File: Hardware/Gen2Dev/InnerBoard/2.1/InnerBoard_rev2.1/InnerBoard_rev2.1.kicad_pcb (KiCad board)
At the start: 2 copper layers, 18 parts, among them J1 SI-46020-F, J2 HMTSW-102-X-X-S-X, J7 USB_C_Receptacle, J8 1051620001, SW1 PTS815 SJM 250 SMTR LFS, SW2 PTS815 SJM 250 SMTR LFS

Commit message: stuff
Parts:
- added C31: 10uF, Capacitor_SMD:C_0805_2012Metric, F.Cu at (188.5, -25.2)
- added D11: LED, LED_SMD:LED_0603_1608Metric, F.Cu at (192.7, -22.6)
- added D12: PMEG6010CEJ, Diode_SMD:D_SOD-323F, F.Cu at (207.1, -45.3)
- added D13: 1N5819WS, Diode_SMD:D_SOD-323, F.Cu at (207.1, -42.3)
- added D14: 1N5819WS, Diode_SMD:D_SOD-323, F.Cu at (207.1, -39.4)
- added J3: UJ31-CH-G2-SMT-TR, UJ31-CH-G2-SMT-TR:CUI_UJ31-CH-G2-SMT-TR, F.Cu at (184.9, -45.1)
- added J4: HMTSW-102-X-X-S-X, HMTSW-102-X-X-S-X:SAMTEC_HMTSW-102-X-X-S-X, F.Cu at (201.7, -32.8)
- added J5: UJ31-CH-G2-SMT-TR, UJ31-CH-G2-SMT-TR:CUI_UJ31-CH-G2-SMT-TR, F.Cu at (196.4, -45.1)
- added J6: HMTSW-102-X-X-S-X, HMTSW-102-X-X-S-X:SAMTEC_HMTSW-102-X-X-S-X, F.Cu at (201.7, -28.7)
- added L6: FB0805/600R/2A, Inductor_SMD:L_0805_2012Metric, F.Cu at (193.0, -25.3)
- added R49: 220, Resistor_SMD:R_0805_2012Metric, F.Cu at (184.0, -33.3)
- added R50: 6.1K, Resistor_SMD:R_0805_2012Metric, F.Cu at (184.0, -30.4)
- added R51: 100, Resistor_SMD:R_0805_2012Metric, F.Cu at (184.0, -27.4)
- added TP1: TestPoint, TestPoint:TestPoint_Pad_D2.0mm, F.Cu at (188.3, -32.8)
- added TP2: TestPoint, TestPoint:TestPoint_Pad_D2.0mm, F.Cu at (188.3, -28.7)
- added TP3: TestPoint, TestPoint:TestPoint_Pad_D2.0mm, F.Cu at (192.3, -32.8)
- added TP4: TestPoint, TestPoint:TestPoint_Pad_D2.0mm, F.Cu at (192.3, -28.7)
- added TP5: TestPoint, TestPoint:TestPoint_Pad_D2.0mm, F.Cu at (196.4, -32.8)
- added TP6: TestPoint, TestPoint:TestPoint_Pad_D2.0mm, F.Cu at (196.4, -28.7)
- added U9: FT232RQ, FT232RQ:QFN50P500X500X90-33N, F.Cu at (202.6, -23.1)
- J7: value USB_C_Receptacle -> HMTSW-102-X-X-S-X; footprint Connector_USB:USB_C_Receptacle_Molex_105450-0101-L -> HMTSW-102-X-X-S-X:SAMTEC_HMTSW-102-X-X-S-X
- R24: value 220R/R0402 -> 0; footprint Resistor_SMD:R_0402_1005Metric -> Resistor_SMD:R_0805_2012Metric
- R26: value 10k/R0402 -> 10k; footprint Resistor_SMD:R_0402_1005Metric -> Resistor_SMD:R_0805_2012Metric
- R27: value NA/R0402 -> 5.1K; footprint Resistor_SMD:R_0402_1005Metric -> Resistor_SMD:R_0805_2012Metric
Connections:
- R24 pad 1: Net-(R24-Pad1) -> /D_Com
- R24 pad 2: GND -> Net-(R24-Pad2)
- R26 pad 2: Net-(R26-Pad2) -> Net-(R24-Pad2)
- R27 pad 1: Net-(R26-Pad2) -> Net-(J5-CC1)
- R27 pad 2: /D_Com -> GND
- SW1 pad 2: Net-(R26-Pad2) -> Net-(R24-Pad2)
- SW1 pad 4: Net-(R24-Pad1) -> Net-(R49-Pad1)
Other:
- board outline added: 101.6 x 76.2 mm

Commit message: stuff
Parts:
- added U11: LAN8710A-EZC, LAN8710A_EZC:QFN32_5X5MC_MCH, F.Cu at (192.3, -53.1)
- added U12: TPS2376PW, TPS2376PW:PW8, F.Cu at (179.4, -52.7)
- added U13: RFM-0505S, RFM_0505S:SIP4_RFM_RCP, F.Cu at (177.7, -64.8)
- added U14: TPS54561DPRR, TPS54561DPRR:WSON10_DPR_TEX, F.Cu at (191.6, -67.5)
- added U15: TPS54561DPRR, TPS54561DPRR:WSON10_DPR_TEX, F.Cu at (191.6, -61.7)
- added U16: ROE-0512S, ROE-0512S:ROE_RCP, F.Cu at (177.7, -60.6)

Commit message: stuff
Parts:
- removed J3: UJ31-CH-G2-SMT-TR, UJ31-CH-G2-SMT-TR:CUI_UJ31-CH-G2-SMT-TR
- removed UEXT1: P-B-V-10-LF, 3221-10-0300-00:CONN10_3221-10-0300-00_CNC
- added C24: 18pF, Capacitor_SMD:C_0402_1005Metric, F.Cu at (136.7, -56.1)
- added C25: 100nF, Capacitor_SMD:C_0805_2012Metric, F.Cu at (133.2, -58.6)
- added C29: 18pF, Capacitor_SMD:C_0402_1005Metric, F.Cu at (136.7, -54.1)
- added C32: 1uF, Capacitor_SMD:C_0805_2012Metric, F.Cu at (186.0, -15.7)
- added D10: 1N5819WS, Diode_SMD:D_SOD-323, F.Cu at (133.2, -55.6)
- added D15: BAT54C, Package_TO_SOT_SMD:SOT-23, F.Cu at (124.2, -62.3)
- added Q4: BC817, Package_TO_SOT_SMD:SOT-23, F.Cu at (124.2, -57.9)
- added Q5: BC817, Package_TO_SOT_SMD:SOT-23, F.Cu at (124.2, -53.4)
- added R34: 2.2k, Resistor_SMD:R_0805_2012Metric, F.Cu at (164.8, -20.1)
- added R35: 10, Resistor_SMD:R_0805_2012Metric, F.Cu at (128.8, -63.1)
- added R41: 1k, Resistor_SMD:R_0805_2012Metric, F.Cu at (128.8, -60.1)
- added R42: 10k, Resistor_SMD:R_0805_2012Metric, F.Cu at (164.8, -17.1)
- added R43: 2.2k, Resistor_SMD:R_0805_2012Metric, F.Cu at (164.8, -14.2)
- added R45: 1k, Resistor_SMD:R_0805_2012Metric, F.Cu at (128.8, -57.2)
- added R46: 220, Resistor_SMD:R_0805_2012Metric, F.Cu at (128.8, -54.2)
- added R47: 10k, Resistor_SMD:R_0805_2012Metric, F.Cu at (164.8, -11.2)
- added R52: 10k, Resistor_SMD:R_0805_2012Metric, F.Cu at (186.0, -12.7)
- added TP7: TestPoint, TestPoint:TestPoint_Pad_D2.0mm, F.Cu at (169.0, -19.5)
- added U10: ESP32-WROOM-32E-N8, ESP32_WROOM_32E_N8:ESP32­WROOM­32E_EXP, F.Cu at (176.3, 124.0)
- added U6: 74LVC1G04, Package_TO_SOT_SMD:SOT-23-5, F.Cu at (133.6, -62.3)
- added Y1: ABLS2-12.000MHZ-D4Y-T, ABLS2-12.000MHZ-D4Y-T:XTAL_ABLS2-12.000MHZ-D4Y-T, F.Cu at (130.0, -67.7)
- J8: value 1051620001 -> 3221-10-0300-00; footprint 1051620001:105162-0001_MOL -> 3221-10-0300-00:CONN10_3221-10-0300-00_CNC
- moved J5 194.4 mm to (97.2, 122.0), turned to -90 degrees
- moved U9 175.4 mm to (108.6, 125.0), turned to -90 degrees
- moved J1 123.9 mm to (102.5, 73.3)
- moved U14 5.12 mm to (195.9, -70.3)
- moved U15 3.66 mm to (195.3, -61.4)
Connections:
- R24 pad 1: /D_Com -> D_Com
- SW1 pad 1: /GPI34/BUT1 -> GPI34/BUT1
- SW2 pad 1: /ESP_EN -> ESP_EN
- U9 pad 27: unconnected-(U9-OSCI-Pad27) -> Net-(U9-OSCI)
- U9 pad 28: unconnected-(U9-OSCO-Pad28) -> Net-(U9-OSCO)
- U9 pad 31: unconnected-(U9-~{DTR}-Pad31) -> Net-(Q5-C)
- U9 pad 32: unconnected-(U9-~{RTS}-Pad32) -> Net-(Q4-E)

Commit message: poe
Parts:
- removed J1: SI-46020-F, SI-46020-F:BEL_SI-46020-F
- removed J7: HMTSW-102-X-X-S-X, HMTSW-102-X-X-S-X:SAMTEC_HMTSW-102-X-X-S-X
- added C20: 10uF, Capacitor_SMD:C_0805_2012Metric, F.Cu at (242.4, -57.8)
- added C21: 1uF, Capacitor_SMD:C_0805_2012Metric, F.Cu at (242.4, -54.8)
- added C22: 10uF, Capacitor_SMD:C_0805_2012Metric, F.Cu at (242.4, -51.8)
- added C23: 1uF, Capacitor_SMD:C_0805_2012Metric, F.Cu at (242.4, -48.8)
- added C59: 1nF, Capacitor_SMD:C_0805_2012Metric, F.Cu at (242.4, -45.8)
- added C60: 22uF, Capacitor_SMD:C_0805_2012Metric, F.Cu at (242.4, -42.8)
- added C61: 100nF, Capacitor_SMD:C_0805_2012Metric, F.Cu at (246.9, -57.8)
- added C62: 100nF, Capacitor_SMD:C_0805_2012Metric, F.Cu at (246.9, -54.8)
- added C63: 2.2uF, Capacitor_SMD:C_0805_2012Metric, F.Cu at (246.9, -51.8)
- added C64: 100nF, Capacitor_SMD:C_0805_2012Metric, F.Cu at (246.9, -48.8)
- added C65: 100nF, Capacitor_SMD:C_0805_2012Metric, F.Cu at (246.9, -45.8)
- added C66: 22uF, Capacitor_SMD:C_0805_2012Metric, F.Cu at (246.9, -42.8)
- added C67: 22uF, Capacitor_SMD:C_0805_2012Metric, F.Cu at (251.3, -57.8)
- added C68: 100nF, Capacitor_SMD:C_0805_2012Metric, F.Cu at (251.3, -54.8)
- added C69: 1nF, Capacitor_SMD:C_0805_2012Metric, F.Cu at (251.3, -51.8)
- added C70: 100nF, Capacitor_SMD:C_0805_2012Metric, F.Cu at (251.3, -48.8)
- added C71: 22uF, Capacitor_SMD:C_0805_2012Metric, F.Cu at (251.3, -45.8)
- added C72: 1uF, Capacitor_SMD:C_0805_2012Metric, F.Cu at (270.0, -54.0)
- added D23: SMAJ58A, Diode_SMD:D_SMA, F.Cu at (233.7, -31.8)
- added D24: BAT54A, Package_TO_SOT_SMD:SOT-23, F.Cu at (270.2, -57.7)
- added D4: LED, LED_SMD:LED_0603_1608Metric, F.Cu at (255.6, -58.1)
- added D5: LED, LED_SMD:LED_0603_1608Metric, F.Cu at (255.6, -55.5)
- added D6: 1N5819, Diode_THT:D_DO-41_SOD81_P10.16mm_Horizontal, F.Cu at (242.1, -39.2)
- added D7: LED, LED_SMD:LED_0603_1608Metric, F.Cu at (255.6, -52.9)
- added J3: HMTSW-102-X-X-S-X, HMTSW-102-X-X-S-X:SAMTEC_HMTSW-102-X-X-S-X, F.Cu at (225.9, -36.7)
- added J9: HMTSW-102-X-X-S-X, HMTSW-102-X-X-S-X:SAMTEC_HMTSW-102-X-X-S-X, F.Cu at (225.9, -32.7)
- added L8: 600R/2A, Inductor_SMD:L_0805_2012Metric, F.Cu at (255.8, -50.2)
- added L9: 600R/2A, Inductor_SMD:L_0805_2012Metric, F.Cu at (255.8, -47.5)
- added Q1: SI2323DS-T1-GE3, SI2323DS-T1-GE3:SOT23, F.Cu at (231.7, -36.4)
- added Q10: BSS138, Package_TO_SOT_SMD:SOT-23, F.Cu at (237.3, -27.3)
- added Q9: SI2323DS-T1-GE3, SI2323DS-T1-GE3:SOT23, F.Cu at (235.7, -36.4)
- added R100: 10k, Resistor_SMD:R_0805_2012Metric, F.Cu at (233.6, -40.2)
- added R101: 10k, Resistor_SMD:R_0805_2012Metric, F.Cu at (238.0, -57.9)
- added R104: 2.2k, Resistor_SMD:R_0805_2012Metric, F.Cu at (238.0, -54.9)
- added R105: 2.2k, Resistor_SMD:R_0805_2012Metric, F.Cu at (238.0, -52.0)
- added R106: 2.2k, Resistor_SMD:R_0805_2012Metric, F.Cu at (238.0, -49.0)
- added R107: 2.2k, Resistor_SMD:R_0805_2012Metric, F.Cu at (238.0, -46.1)
- added R108: 49.9k, Resistor_SMD:R_0805_2012Metric, F.Cu at (265.5, -58.5)
- added R109: 100k, Resistor_SMD:R_0805_2012Metric, F.Cu at (265.5, -55.5)
- added R21: 10k, Resistor_SMD:R_0805_2012Metric, F.Cu at (224.8, -57.9)
- added R22: 2.2k, Resistor_SMD:R_0805_2012Metric, F.Cu at (224.8, -54.9)
- added R23: 100, Resistor_SMD:R_0805_2012Metric, F.Cu at (224.8, -52.0)
- added R25: 100, Resistor_SMD:R_0805_2012Metric, F.Cu at (224.8, -49.0)
- added R28: 100, Resistor_SMD:R_0805_2012Metric, F.Cu at (224.8, -46.1)
- added R29: 2.2k, Resistor_SMD:R_0805_2012Metric, F.Cu at (224.8, -43.1)
- added R30: 10k, Resistor_SMD:R_0805_2012Metric, F.Cu at (224.8, -40.2)
- added R31: 12.1k, Resistor_SMD:R_0805_2012Metric, F.Cu at (229.2, -57.9)
- added R32: 1k, Resistor_SMD:R_0805_2012Metric, F.Cu at (229.2, -54.9)
- added R33: 49.9, Resistor_SMD:R_0805_2012Metric, F.Cu at (229.2, -52.0)
- added R81: 49.9, Resistor_SMD:R_0805_2012Metric, F.Cu at (229.2, -49.0)
- added R82: 49.9, Resistor_SMD:R_0805_2012Metric, F.Cu at (229.2, -46.1)
- added R83: 49.9, Resistor_SMD:R_0805_2012Metric, F.Cu at (229.2, -43.1)
- added R84: 220, Resistor_SMD:R_0805_2012Metric, F.Cu at (229.2, -40.2)
- added R89: 220, Resistor_SMD:R_0805_2012Metric, F.Cu at (233.6, -57.9)
- added R90: 24.9k, Resistor_SMD:R_0805_2012Metric, F.Cu at (233.6, -54.9)
- added R93: 180k, Resistor_SMD:R_0805_2012Metric, F.Cu at (233.6, -52.0)
- added R94: 4.42k, Resistor_SMD:R_0805_2012Metric, F.Cu at (233.6, -49.0)
- added R97: 10k, Resistor_SMD:R_0805_2012Metric, F.Cu at (233.6, -46.1)
- added R99: 1k, Resistor_SMD:R_0805_2012Metric, F.Cu at (233.6, -43.1)
- added U23: ESDS314DBVR, ESDS314DBVR:DBV0005A_N, F.Cu at (225.2, -28.3)
- added U4: MIC5504-3.3YM5, Package_TO_SOT_SMD:SOT-23-5, F.Cu at (232.2, -27.3)
- added U7: LD1117S50TR_SOT223, Package_TO_SOT_SMD:SOT-223-3_TabPin2, F.Cu at (245.1, -32.9)
- added Y3: ASV-50.000MHZ-LCS-T, ASV-50.000MHZ-LCS-T:XTAL_ASV-50.000MHZ-LCS-T, F.Cu at (254.4, -32.8)
- J6: value HMTSW-102-X-X-S-X -> SI-46020-F; footprint HMTSW-102-X-X-S-X:SAMTEC_HMTSW-102-X-X-S-X -> SI-46020-F:BEL_SI-46020-F
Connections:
- U11 pad 1: unconnected-(U11-VDD2A-Pad1) -> VDDA1/2
- U11 pad 10: unconnected-(U11-RXD1/*MODE1-Pad10) -> GPIO26/EMAC_RXD1(RMII)
- U11 pad 11: unconnected-(U11-RXD0/*MODE0-Pad11) -> GPIO25/EMAC_RXD0(RMII)
- U11 pad 12: unconnected-(U11-VDDIO-Pad12) -> +3.3VLAN
- U11 pad 13: unconnected-(U11-RXER/RXD4/*PHYAD0-Pad13) -> PHYAD0
- U11 pad 15: unconnected-(U11-COL/CRS_DV/*MODE2-Pad15) -> GPIO27/EMAC_RX_CRS_DV
- U11 pad 16: unconnected-(U11-MDIO-Pad16) -> GPIO18/MDIO(RMII)
- U11 pad 17: unconnected-(U11-MDC-Pad17) -> GPIO23/MDC(RMII)
- U11 pad 19: unconnected-(U11-NRST-Pad19) -> Net-(JP1-B)
- U11 pad 2: unconnected-(U11-LED2/*NINTSEL-Pad2) -> LED2
- U11 pad 21: unconnected-(U11-TXEN-Pad21) -> GPIO21/EMAC_TX_EN(RMII)
- U11 pad 22: unconnected-(U11-TXD0-Pad22) -> GPIO19/EMAC_TXD0(RMII)
- U11 pad 23: unconnected-(U11-TXD1-Pad23) -> GPIO22/EMAC_TXD1(RMII)
- U11 pad 24: unconnected-(U11-TXD2-Pad24) -> GND
- U11 pad 25: unconnected-(U11-TXD3-Pad25) -> GND
- U11 pad 27: unconnected-(U11-VDD1A-Pad27) -> VDDA1/2
- U11 pad 28: unconnected-(U11-TXN-Pad28) -> Net-(J6-TD-)
- U11 pad 29: unconnected-(U11-TXP-Pad29) -> Net-(J6-TD+)
- U11 pad 3: unconnected-(U11-LED1/*REGOFF-Pad3) -> LED1
- U11 pad 30: unconnected-(U11-RXN-Pad30) -> Net-(J6-RD-)
- U11 pad 31: unconnected-(U11-RXP-Pad31) -> Net-(J6-RD+)
- U11 pad 32: unconnected-(U11-RBIAS-Pad32) -> Net-(U11-RBIAS)
- U11 pad 33: unconnected-(U11-EPAD-Pad33) -> Net-(U11-EPAD)
- U11 pad 5: unconnected-(U11-XTAL1/CLKIN-Pad5) -> GPIO0/XTAL1/CLKIN
- U11 pad 6: unconnected-(U11-VDDCR-Pad6) -> Net-(U11-VDDCR)
- U11 pad 7: unconnected-(U11-RXCLK/*PHYAD1-Pad7) -> PHYAD1
- U11 pad 8: unconnected-(U11-RXD3/*PHYAD2-Pad8) -> PHYAD2
- U11 pad 9: unconnected-(U11-RXD2/*RMIISEL-Pad9) -> RMIISEL
- U12 pad 1: unconnected-(U12-ILIM-Pad1) -> Net-(U12-ILIM)
- U12 pad 2: unconnected-(U12-CLASS-Pad2) -> Net-(U12-CLASS)
- U12 pad 3: unconnected-(U12-DET-Pad3) -> Net-(U12-DET)
- U12 pad 4: unconnected-(U12-VSS-Pad4) -> Spare2
- U12 pad 8: unconnected-(U12-VDD-Pad8) -> Spare1

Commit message: stuff
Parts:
- removed U14, U15: TPS54561DPRR, TPS54561DPRR:WSON10_DPR_TEX
- added C1: 15uF, Capacitor_SMD:C_0805_2012Metric, F.Cu at (204.3, -75.7)
- added C2: 100pF, Capacitor_SMD:C_0805_2012Metric, F.Cu at (204.3, -72.7)
- added C3: 220nF, Capacitor_SMD:C_0805_2012Metric, F.Cu at (204.3, -69.7)
- added C4: 470pF, Capacitor_SMD:C_0805_2012Metric, F.Cu at (204.3, -66.7)
- added C5: 12nF, Capacitor_SMD:C_0805_2012Metric, F.Cu at (204.3, -63.7)
- added C6: 100nF, Capacitor_SMD:C_0805_2012Metric, F.Cu at (204.3, -60.6)
- added C7: 1uF, Capacitor_SMD:C_0805_2012Metric, F.Cu at (204.3, -57.6)
- added C8: 100pF, Capacitor_SMD:C_0805_2012Metric, F.Cu at (204.3, -54.6)
- added R1: 130k, Resistor_SMD:R_0805_2012Metric, F.Cu at (208.8, -75.7)
- added R2: 10k, Resistor_SMD:R_0805_2012Metric, F.Cu at (208.8, -72.8)
- added R3: 18k, Resistor_SMD:R_0805_2012Metric, F.Cu at (208.8, -69.8)
- added R4: 8.25k, Resistor_SMD:R_0805_2012Metric, F.Cu at (208.8, -66.9)
- added R5: 9.3k, Resistor_SMD:R_0805_2012Metric, F.Cu at (208.8, -63.9)
- added R6: 6k, Resistor_SMD:R_0805_2012Metric, F.Cu at (208.8, -61.0)
- added R7: 100, Resistor_SMD:R_0805_2012Metric, F.Cu at (208.8, -58.0)
- added R8: 5.24M, Resistor_SMD:R_0805_2012Metric, F.Cu at (208.8, -55.1)
- added U1: LM5156DSSR, LM5156DSSR:DSS0012B, F.Cu at (212.7, -75.1)
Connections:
- C20 pad 2: GND -> Spare2
- C21 pad 2: GND -> Spare2
- C22 pad 2: GND -> Spare2
- C23 pad 2: GND -> Spare2
- C24 pad 1: GND -> Spare2
- C25 pad 2: GND -> Spare2
- C29 pad 1: GND -> Spare2
- C31 pad 2: GND -> Spare2
- C32 pad 2: GND -> Spare2
- C59 pad 2: GND -> Spare2
- C63 pad 2: GND -> Spare2
- C64 pad 2: GND -> Spare2
- C65 pad 2: GND -> Spare2
- C66 pad 2: GND -> Spare2
- C67 pad 2: GND -> Spare2
- C68 pad 2: GND -> Spare2
- C69 pad 2: GND -> Spare2
- C72 pad 2: GND -> Spare2
- D11 pad 1: GND -> Spare2
- D4 pad 1: GND -> Spare2
- D5 pad 1: GND -> Spare2
- D7 pad 1: GND -> Spare2
- J2 pad 02: GND -> Spare2
- J6 pad 10: Spare2 -> Spare1
- J6 pad 9: Spare1 -> Spare2
- J8 pad 1: GND -> Spare2
- L6 pad 2: GND -> Spare2
- Q10 pad 2: GND -> Spare2
- R104 pad 2: GND -> Spare2
- R105 pad 2: GND -> Spare2
- R106 pad 2: GND -> Spare2
- R21 pad 1: GND -> Spare2
- R27 pad 2: GND -> Spare2
- R31 pad 1: GND -> Spare2
- R49 pad 2: GND -> Spare2
- R50 pad 2: GND -> Spare2
- R89 pad 1: GND -> Spare2
- SW2 pad 4: GND -> Spare2
- U10 pad 1: GND -> Spare2
- U10 pad 38: GND -> Spare2
- U10 pad 39: GND -> Spare2
- U10 pad 40: GND -> Spare2
- U10 pad 41: GND -> Spare2
- U10 pad 42: GND -> Spare2
- U10 pad 43: GND -> Spare2
- U10 pad 44: GND -> Spare2
- U10 pad 45: GND -> Spare2
- U10 pad 46: GND -> Spare2
- U10 pad 47: GND -> Spare2
- U11 pad 24: GND -> Spare2
- U11 pad 25: GND -> Spare2
- U12 pad 5: unconnected-(U12-RTN-Pad5) -> Spare2
- U12 pad 7: unconnected-(U12-UVLO-Pad7) -> Net-(U12-UVLO)
- U23 pad 2: GND -> Spare2
- U4 pad 2: GND -> Spare2
- U6 pad 5: GND -> Spare2
- U7 pad 1: GND -> Spare2
- U9 pad 17: GND -> Spare2
- U9 pad 20: GND -> Spare2
- U9 pad 24: GND -> Spare2
- U9 pad 4: GND -> Spare2
- Y3 pad 2: GND -> Spare2

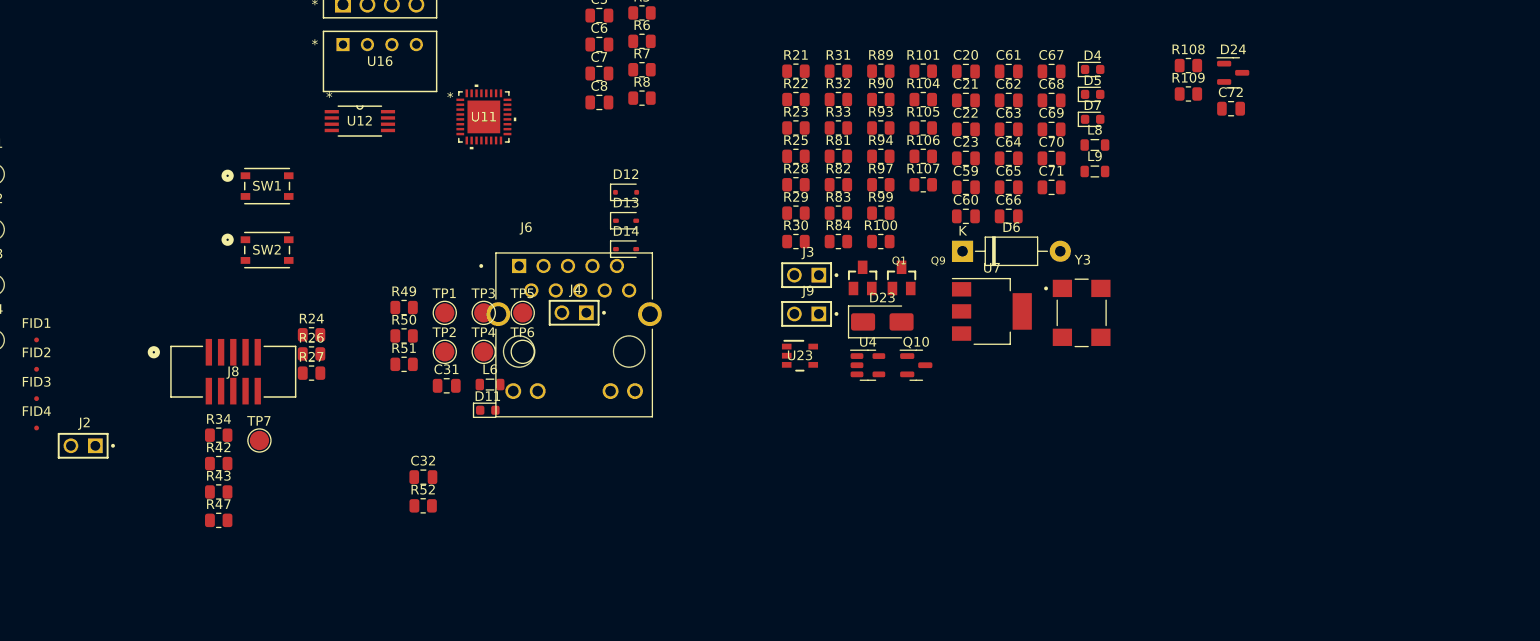
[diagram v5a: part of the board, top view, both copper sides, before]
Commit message: schematic for v2.1 dev board done. Footprints update progress. Layout will roll when footprints finalize
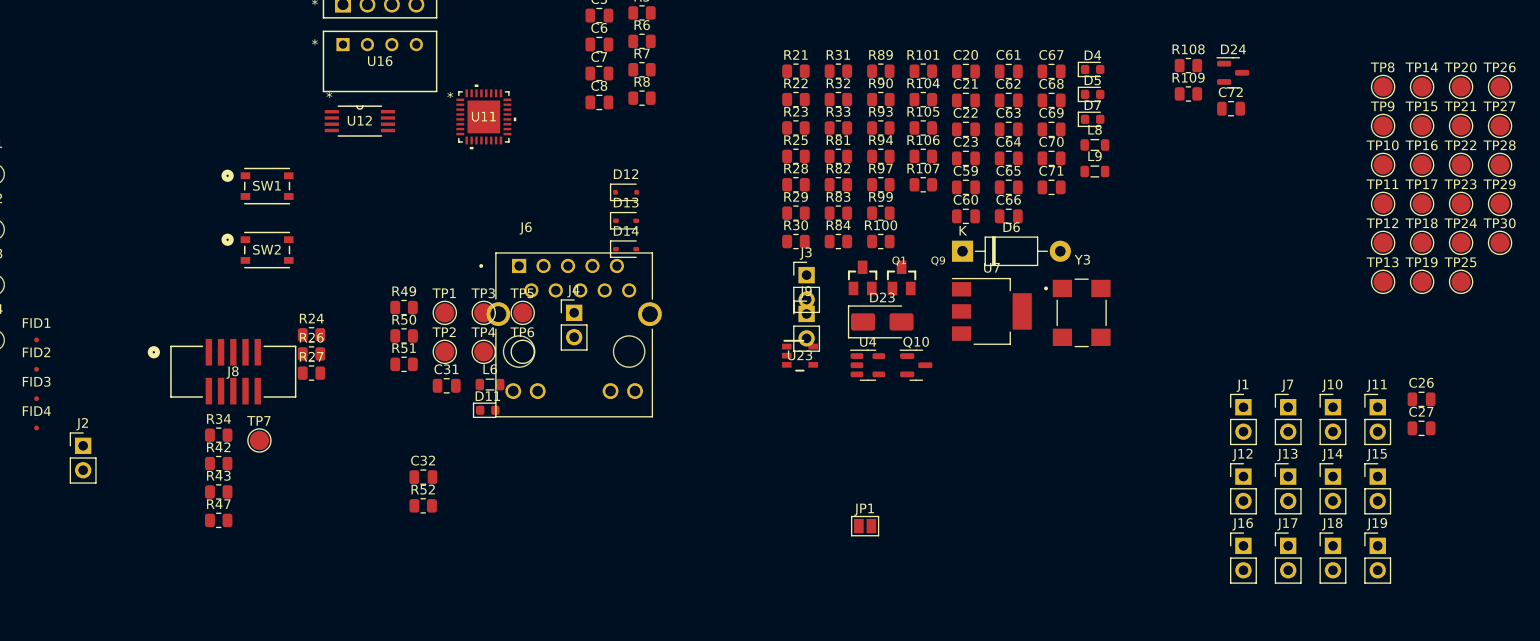
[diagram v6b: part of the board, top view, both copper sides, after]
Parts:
- added C26: 100nF, Capacitor_SMD:C_0805_2012Metric, F.Cu at (289.8, -23.8)
- added C27: 10uF, Capacitor_SMD:C_0805_2012Metric, F.Cu at (289.8, -20.8)
- added J1: HMTSW-102-X-X-S-X, Connector_PinHeader_2.54mm:PinHeader_1x02_P2.54mm_Vertical, F.Cu at (271.2, -23.0)
- added J10: HMTSW-102-X-X-S-X, Connector_PinHeader_2.54mm:PinHeader_1x02_P2.54mm_Vertical, F.Cu at (280.6, -23.0)
- added J11: HMTSW-102-X-X-S-X, Connector_PinHeader_2.54mm:PinHeader_1x02_P2.54mm_Vertical, F.Cu at (285.2, -23.0)
- added J12: HMTSW-102-X-X-S-X, Connector_PinHeader_2.54mm:PinHeader_1x02_P2.54mm_Vertical, F.Cu at (271.2, -15.8)
- added J13: HMTSW-102-X-X-S-X, Connector_PinHeader_2.54mm:PinHeader_1x02_P2.54mm_Vertical, F.Cu at (275.9, -15.8)
- added J14: HMTSW-102-X-X-S-X, Connector_PinHeader_2.54mm:PinHeader_1x02_P2.54mm_Vertical, F.Cu at (280.6, -15.8)
- added J15: HMTSW-102-X-X-S-X, Connector_PinHeader_2.54mm:PinHeader_1x02_P2.54mm_Vertical, F.Cu at (285.2, -15.8)
- added J16: HMTSW-102-X-X-S-X, Connector_PinHeader_2.54mm:PinHeader_1x02_P2.54mm_Vertical, F.Cu at (271.2, -8.56)
- added J17: HMTSW-102-X-X-S-X, Connector_PinHeader_2.54mm:PinHeader_1x02_P2.54mm_Vertical, F.Cu at (275.9, -8.56)
- added J18: HMTSW-102-X-X-S-X, Connector_PinHeader_2.54mm:PinHeader_1x02_P2.54mm_Vertical, F.Cu at (280.6, -8.56)
- added J19: HMTSW-102-X-X-S-X, Connector_PinHeader_2.54mm:PinHeader_1x02_P2.54mm_Vertical, F.Cu at (285.2, -8.56)
- added J7: HMTSW-102-X-X-S-X, Connector_PinHeader_2.54mm:PinHeader_1x02_P2.54mm_Vertical, F.Cu at (275.9, -23.0)
- added JP1: SolderJumper_2_Open, Jumper:SolderJumper-2_P1.3mm_Open_Pad1.0x1.5mm, F.Cu at (231.9, -10.6)
- added TP10: TestPoint, TestPoint:TestPoint_Pad_D2.0mm, F.Cu at (285.8, -48.1)
- added TP11: TestPoint, TestPoint:TestPoint_Pad_D2.0mm, F.Cu at (285.8, -44.1)
- added TP12: TestPoint, TestPoint:TestPoint_Pad_D2.0mm, F.Cu at (285.8, -40.0)
- added TP13: TestPoint, TestPoint:TestPoint_Pad_D2.0mm, F.Cu at (285.8, -36.0)
- added TP14: TestPoint, TestPoint:TestPoint_Pad_D2.0mm, F.Cu at (289.8, -56.2)
- added TP15: TestPoint, TestPoint:TestPoint_Pad_D2.0mm, F.Cu at (289.8, -52.2)
- added TP16: TestPoint, TestPoint:TestPoint_Pad_D2.0mm, F.Cu at (289.8, -48.1)
- added TP17: TestPoint, TestPoint:TestPoint_Pad_D2.0mm, F.Cu at (289.8, -44.1)
- added TP18: TestPoint, TestPoint:TestPoint_Pad_D2.0mm, F.Cu at (289.8, -40.0)
- added TP19: TestPoint, TestPoint:TestPoint_Pad_D2.0mm, F.Cu at (289.8, -36.0)
- added TP20: TestPoint, TestPoint:TestPoint_Pad_D2.0mm, F.Cu at (293.9, -56.2)
- added TP21: TestPoint, TestPoint:TestPoint_Pad_D2.0mm, F.Cu at (293.9, -52.2)
- added TP22: TestPoint, TestPoint:TestPoint_Pad_D2.0mm, F.Cu at (293.9, -48.1)
- added TP23: TestPoint, TestPoint:TestPoint_Pad_D2.0mm, F.Cu at (293.9, -44.1)
- added TP24: TestPoint, TestPoint:TestPoint_Pad_D2.0mm, F.Cu at (293.9, -40.0)
- added TP25: TestPoint, TestPoint:TestPoint_Pad_D2.0mm, F.Cu at (293.9, -36.0)
- added TP26: TestPoint, TestPoint:TestPoint_Pad_D2.0mm, F.Cu at (297.9, -56.2)
- added TP27: TestPoint, TestPoint:TestPoint_Pad_D2.0mm, F.Cu at (297.9, -52.2)
- added TP28: TestPoint, TestPoint:TestPoint_Pad_D2.0mm, F.Cu at (297.9, -48.1)
- added TP29: TestPoint, TestPoint:TestPoint_Pad_D2.0mm, F.Cu at (297.9, -44.1)
- added TP30: TestPoint, TestPoint:TestPoint_Pad_D2.0mm, F.Cu at (297.9, -40.0)
- added TP8: TestPoint, TestPoint:TestPoint_Pad_D2.0mm, F.Cu at (285.8, -56.2)
- added TP9: TestPoint, TestPoint:TestPoint_Pad_D2.0mm, F.Cu at (285.8, -52.2)
- J2, J3, J4, J9: footprint HMTSW-102-X-X-S-X:SAMTEC_HMTSW-102-X-X-S-X -> Connector_PinHeader_2.54mm:PinHeader_1x02_P2.54mm_Vertical
- R50: value 6.1K -> 5.1K
- U1: footprint LM5156DSSR:DSS0012B -> 5156:DSS0012B
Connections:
- J5 pad A1: Net-(J5-GND) -> Spare2
- J5 pad A12: Net-(J5-GND) -> Spare2
- J5 pad A6: USB_DN -> USB_DP
- J5 pad B1: Net-(J5-GND) -> Spare2
- J5 pad B12: Net-(J5-GND) -> Spare2
- J5 pad B7: USB_DP -> USB_DN
- J5 pad SH1: Net-(J5-GND) -> Spare2
- J5 pad SH2: Net-(J5-GND) -> Spare2
- J5 pad SH3: Net-(J5-GND) -> Spare2
- J5 pad SH4: Net-(J5-GND) -> Spare2
- R104 pad 1: PHYAD0 -> Net-(J13-Pad02)
- R105 pad 1: PHYAD1 -> Net-(J14-Pad02)
- R106 pad 1: PHYAD2 -> Net-(J15-Pad02)
- U9 pad 14: USB_DP -> Net-(U9-USBDP)
- U9 pad 15: USB_DN -> Net-(U9-USBDM)
